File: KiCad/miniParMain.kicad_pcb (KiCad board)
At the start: 4 copper layers, 25 x 40 mm, 30 parts, among them J2 USB_C_Receptacle, J4 Conn_01x02_Pin, J5 secondBoard, SW2 SW_Push, U1 AS7341-DLGT, U2 IP4234CZ6, U5 AP7312-1833W6-7, U8 ESP8685, Y2 40MHz

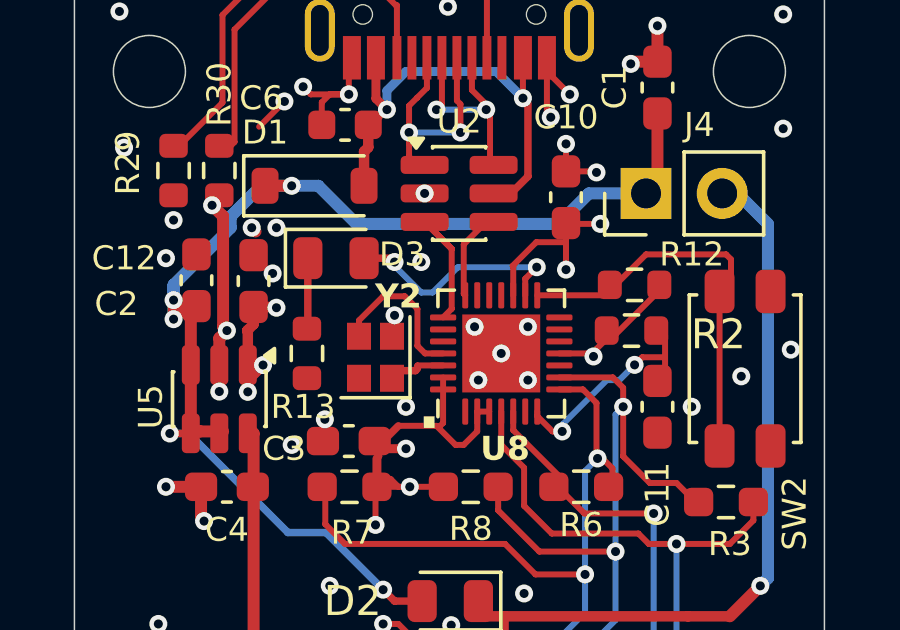
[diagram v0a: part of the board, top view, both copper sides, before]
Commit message: clean up of schematics - mpn + bom
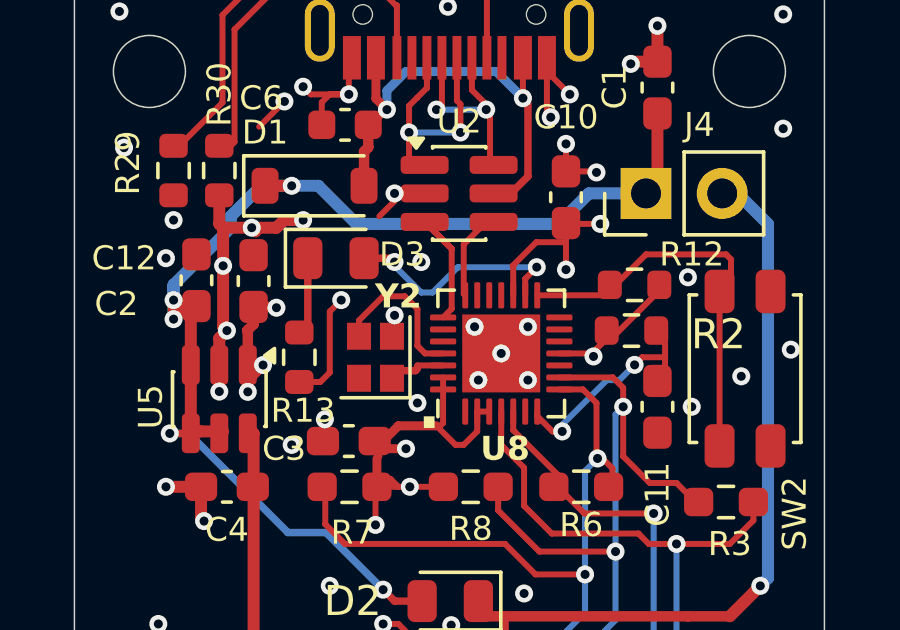
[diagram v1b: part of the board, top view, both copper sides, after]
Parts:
- R2: value 10K -> 5.1K
- moved R13 0.28 mm to (95.0, 89.0)
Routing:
- net GND: track 28.0 -> 35.7 mm, vias 52 -> 53
